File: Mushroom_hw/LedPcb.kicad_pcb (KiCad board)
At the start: 2 copper layers, 8.6 x 8 mm, 6 parts, among them Q1 LED_RGB, Q2 LED_RGB_WS2812B

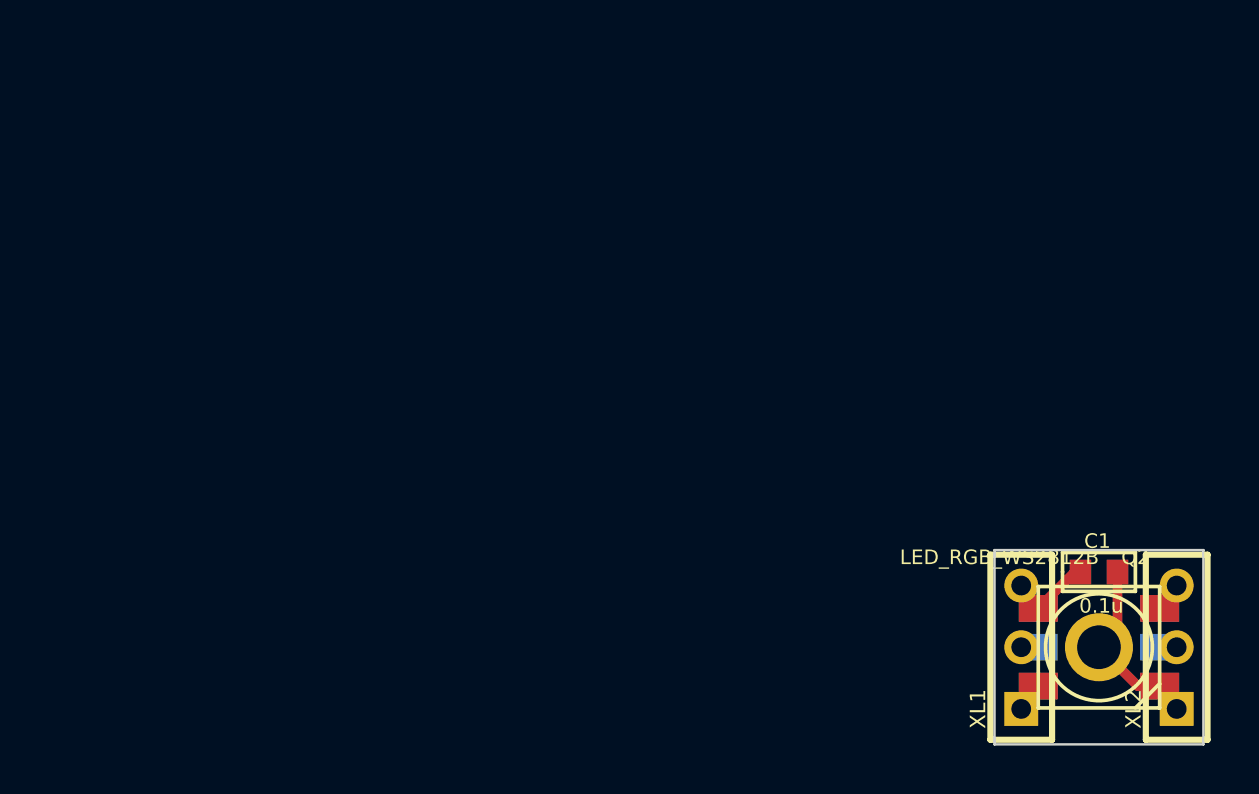
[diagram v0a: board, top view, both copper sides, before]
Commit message: + New LedPcb (WS2812 only)
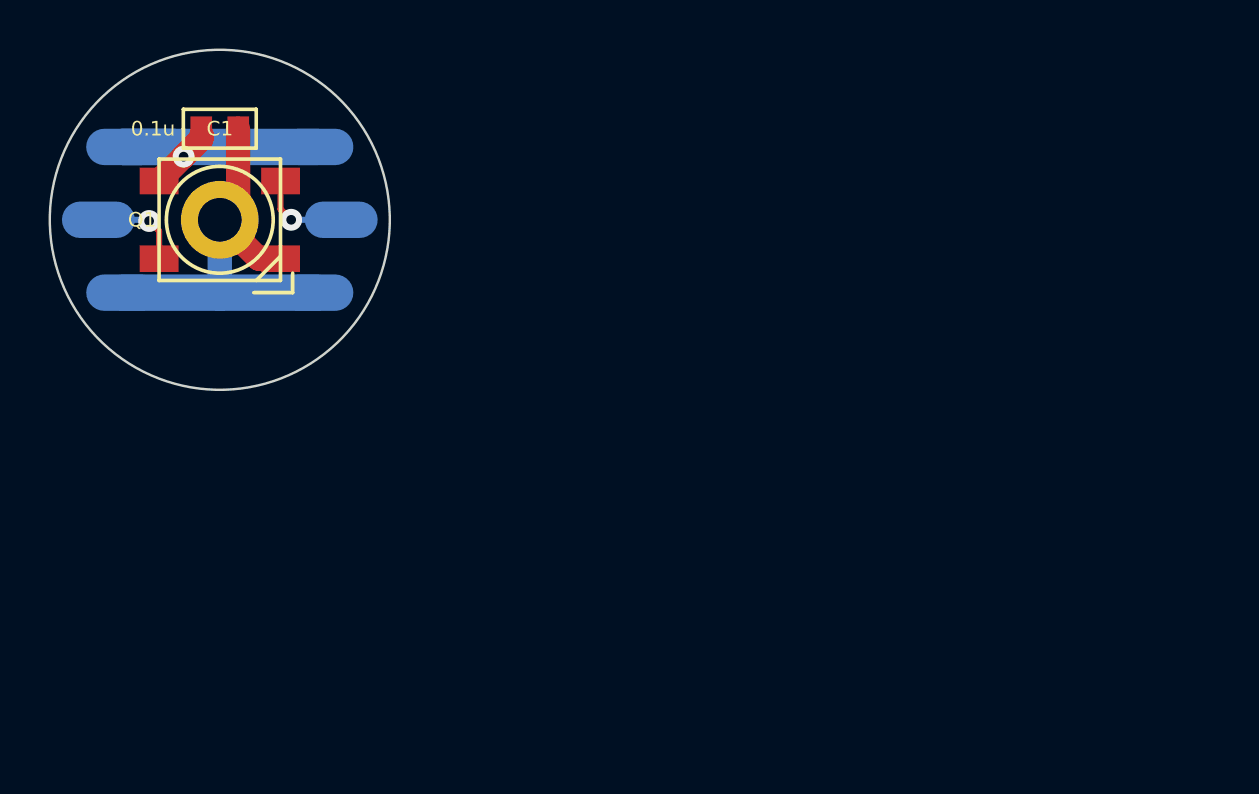
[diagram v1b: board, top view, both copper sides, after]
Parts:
- removed Q2: LED_RGB_WS2812B, LED_WS2812B
- added HOLE1: HOLE_METALLED, PCB:Hole1d8_out3d2mm, F.Cu at (122.0, 83.0)
- added XL4: CONN_1, PCB:Oval3x1.5, B.Cu at (117.0, 83.0)
- added XL5: CONN_1, PCB:Oval3x1.5, B.Cu at (118.0, 86.0)
- added XL6: CONN_1, PCB:Oval3x1.5, B.Cu at (126.0, 86.0)
- C1: footprint CAP_0603 -> Capacitors:CAP_0603
- Q1: value LED_RGB -> LED_RGB_WS2812B; footprint LED_HH5050_RGB -> LEDs:LED_WS2812B; moved to F.Cu
- XL1, XL2: value CONN_3 -> CONN_1; footprint SIL-3 -> PCB:Oval3x1.5; moved to B.Cu
- XL3: footprint SIL1_ROUND_1MM8 -> PCB:Oval3x1.5; moved to B.Cu
- moved XL2 48.0 mm to (118.0, 80.0), turned to 0 degrees
- moved C1 40.5 mm to (122.0, 79.2)
- moved Q1 40.3 mm to (122.0, 83.0)
- moved XL3 38.2 mm to (126.0, 80.0)
- moved XL1 33.1 mm to (127.0, 83.0), turned to 0 degrees
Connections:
- C1 pad 1: N-000006 -> /VDD
- C1 pad 2: N-000007 -> /GND
- XL1 pad 1: N-000001 -> /DIN
- XL2 pad 1: N-000005 -> /VDD
- XL3 pad 1: N-000007 -> /VDD
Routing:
- net /GND: track 0.00 -> 18.2 mm
- net /VDD: track 0.00 -> 14.5 mm, vias 0 -> 1
- net N-000007: track 7.91 -> 0.00 mm
- net /DIN: track 0.00 -> 3.84 mm, vias 0 -> 1
- net /DOUT: track 0.00 -> 3.83 mm, vias 0 -> 1
- net N-000006: track 3.63 -> 0.00 mm
- net N-000005: track 1.23 -> 0.00 mm
- net N-000002: track 1.23 -> 0.00 mm
- net N-000001: track 1.23 -> 0.00 mm
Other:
- board size 8.6 x 8 mm -> 14 x 14 mm
- net class Default: clearance 0.2 -> 0.22; trace_width 0.4 -> 0.254; via_dia 0.889 -> 0.9; via_drill 0.635 -> 0.4
- net class Wide added: clearance 0.22, trace_width 1.5, via_dia 0.9, via_drill 0.4
- rule trace_clearance: 0.2 -> 0.22
- rule trace_min: 0.254 -> 0.2
- rule via_min_drill: 0.508 -> 0.2
- board text added: "+Vdd"
- board text added: "GND"
- board text added: "In"
- board text added: "Out"
